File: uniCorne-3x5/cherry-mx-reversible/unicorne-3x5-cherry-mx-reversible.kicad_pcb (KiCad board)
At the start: 2 copper layers, 114.7 x 91.4 mm, 87 parts, among them J1 MJ-4PP-9, J2 Nice!View, J3 Conn_01x02, J4 Conn_01x03, SW1 SW_MX_HS, SW10 SW_MX_HS, SW11 SW_MX_HS, SW12 SW_MX_HS, SW13 SW_MX_HS, SW14 SW_MX_HS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

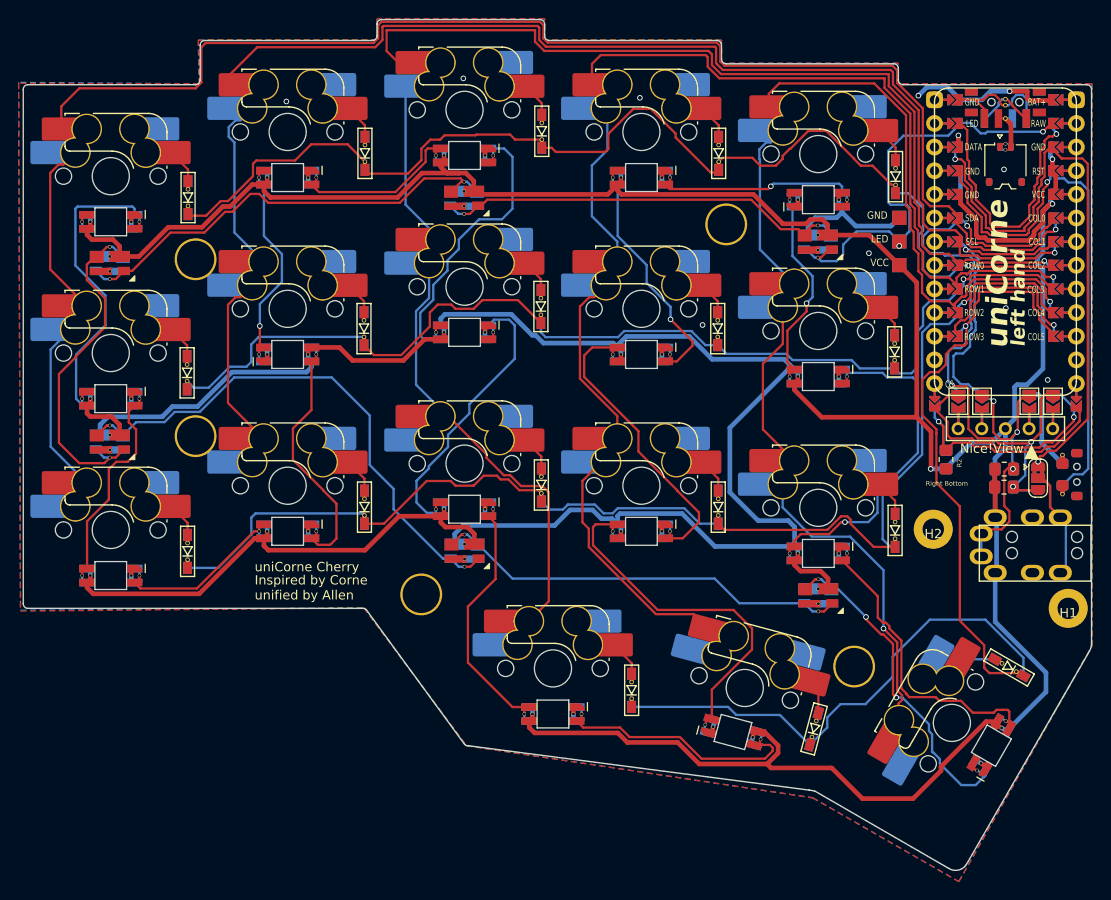
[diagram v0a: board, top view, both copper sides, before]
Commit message: amended cherry mx 3x5
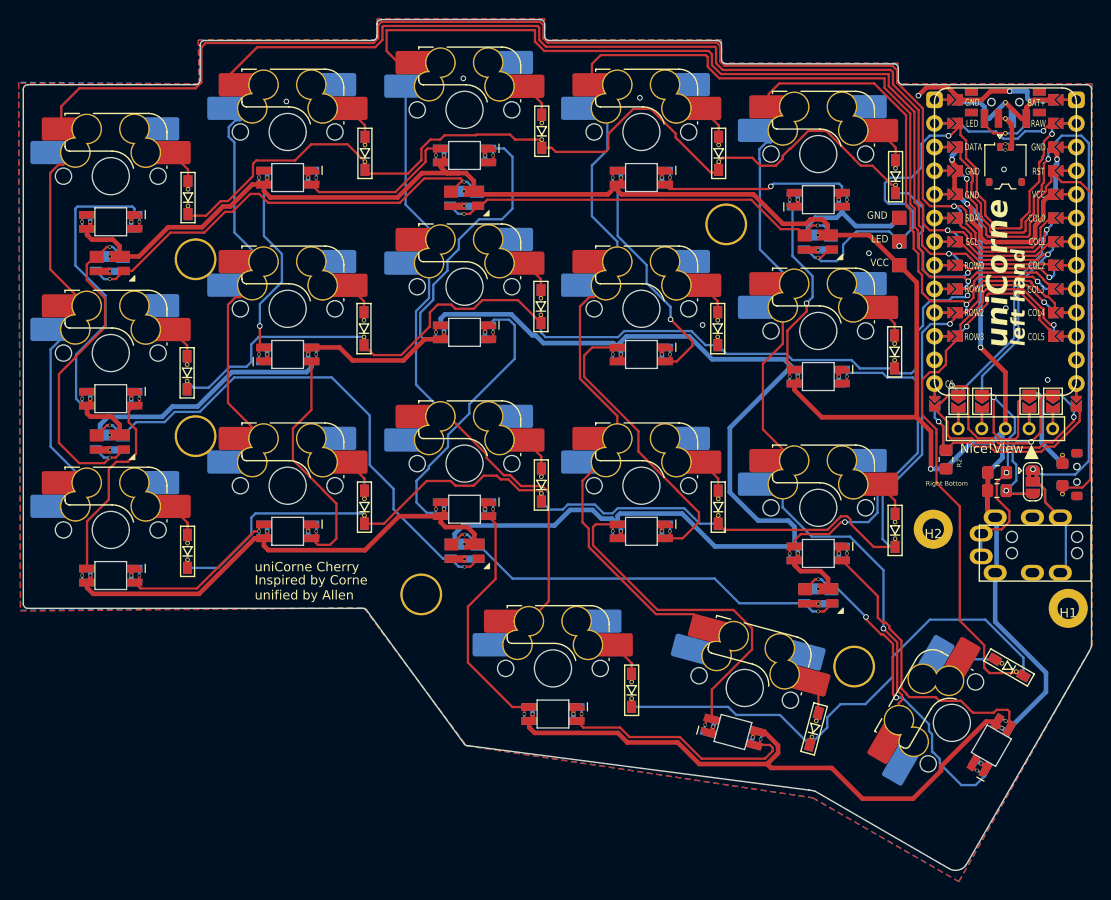
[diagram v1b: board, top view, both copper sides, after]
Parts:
- U1: footprint TB2086_MISC:ProMicro-ish-dn-rev-unrouted_3x5 -> TB2086_MISC:ProMicro-ish-dn-rev-unrouted_3x6
- moved R3 0.85 mm to (184.6, 109.8)
- moved R4 0.85 mm to (184.5, 111.7)
- moved JP9 0.70 mm to (188.4, 110.8)
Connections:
- PSW1 pad 1: unconnected-(PSW1-A-Pad1) -> BAT+
- PSW1 pad 3: BAT+ -> unconnected-(PSW1-C-Pad3)
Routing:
- net LED: track 46.5 -> 64.9 mm, vias 2 -> 3
- net unconnected-(U1-RAW-Pad24): track 28.3 -> 11.0 mm
- net unconnected-(PSW1-C-Pad3): track 0.00 -> 6.54 mm
- net unconnected-(PSW1-A-Pad1): track 6.23 -> 0.00 mm
- net DATA: track 64.8 -> 70.5 mm
- net SCL: track 60.3 -> 64.7 mm, vias 4 -> 3
- net GND: track 34.8 -> 38.3 mm
- net row0: track 123.0 -> 126.3 mm, vias 1 -> 2
- net BAT+: track 17.4 -> 14.2 mm
- net unconnected-(U1-B3-Pad15): track 18.6 -> 15.8 mm
- net row3: track 117.9 -> 115.6 mm
- net RESET: track 58.8 -> 60.3 mm
- net SDA: track 72.5 -> 71.1 mm
- net col2: track 166.6 -> 167.8 mm
- net col3: track 143.3 -> 142.4 mm
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
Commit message: amended chocolate 3x5
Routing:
- net SDA: track 71.1 -> 70.0 mm
- net row2: track 131.9 -> 131.2 mm
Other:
- board text added: "uniCorne Cherry 3x5"
- board text removed: "uniCorne Cherry"

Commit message: small tweak
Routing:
- net DATA: track 70.5 -> 76.6 mm
- net RESET: track 60.3 -> 62.9 mm
- net SDA: track 70.0 -> 68.6 mm
- net unconnected-(PSW1-C-Pad3): track 6.54 -> 5.31 mm
- net SCL: track 64.7 -> 63.6 mm
- net Net-(JP9-C): track 15.4 -> 14.5 mm
- net row0: track 126.3 -> 125.7 mm
- net col2: track 167.8 -> 167.2 mm

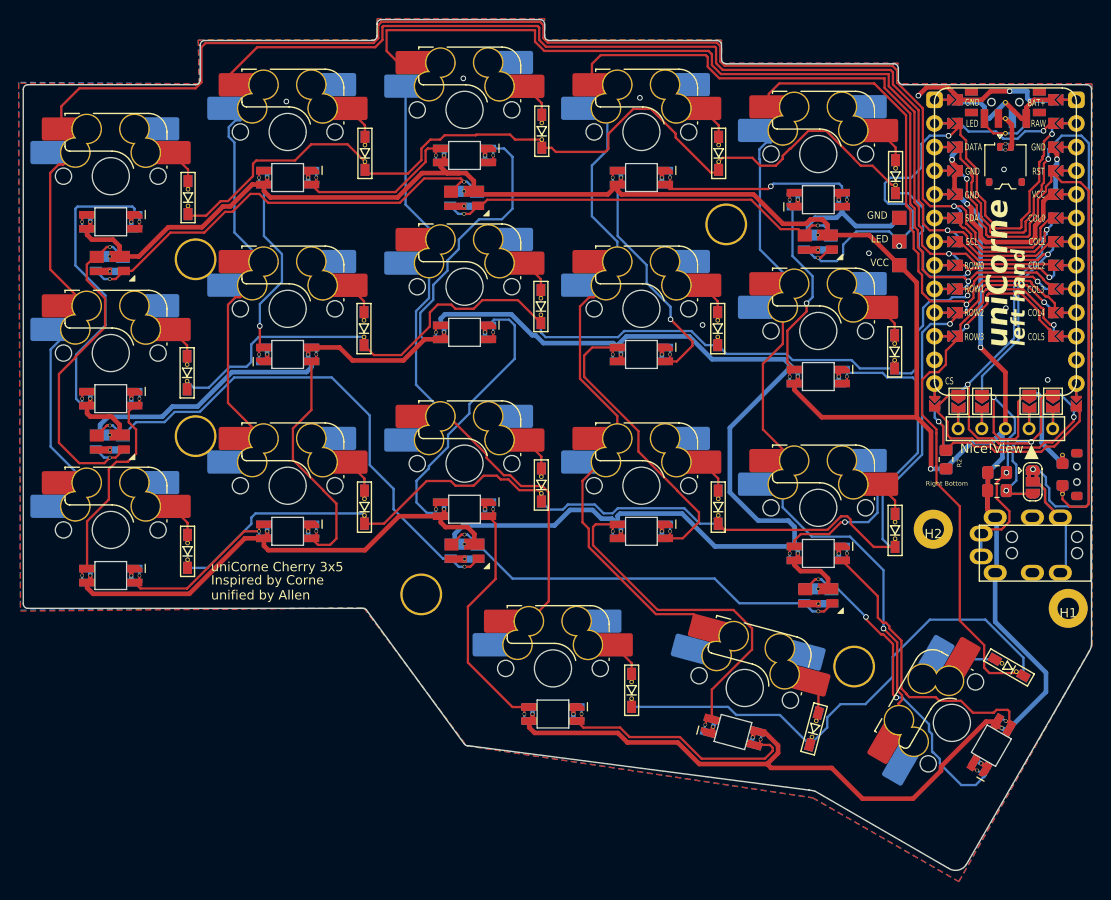
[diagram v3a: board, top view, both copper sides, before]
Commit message: amended footprint for LED
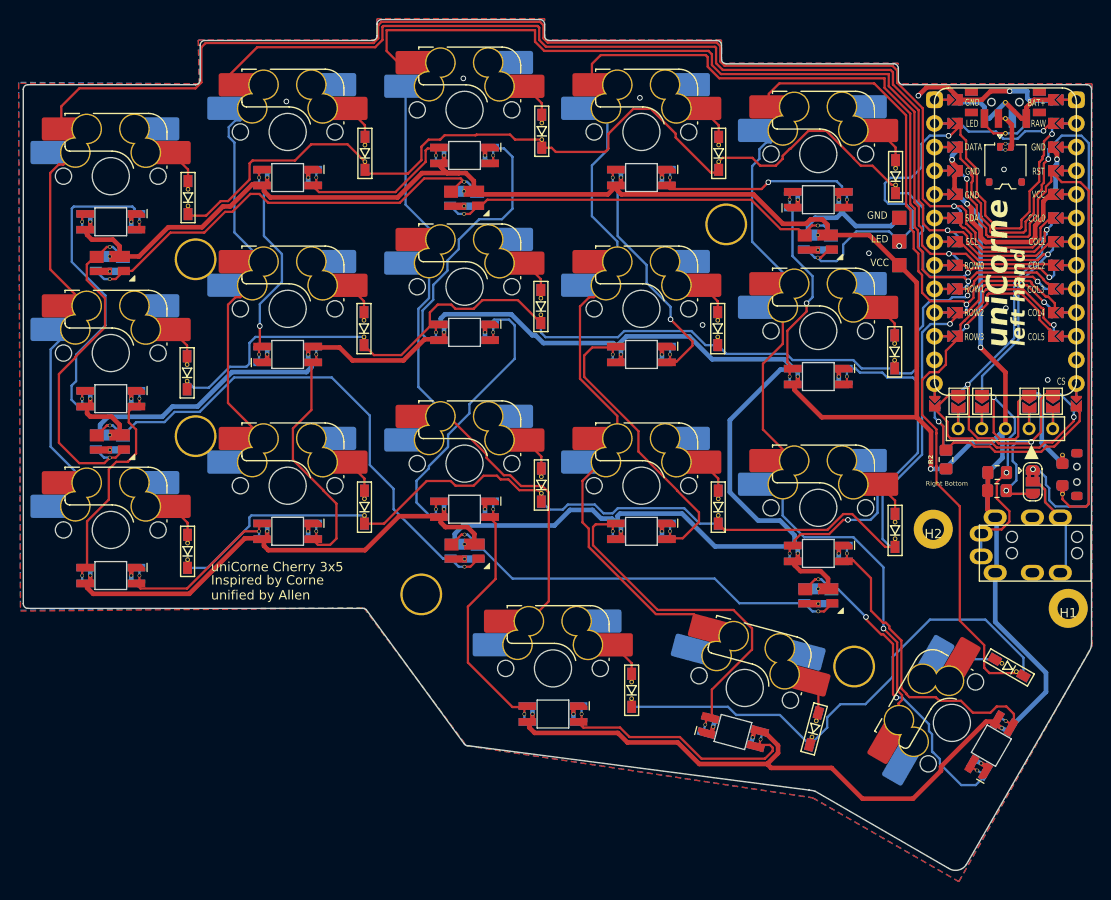
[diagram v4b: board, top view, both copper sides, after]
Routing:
- net Net-(L15-DIN): track 31.3 -> 32.9 mm
- net col4: track 131.7 -> 133.0 mm
- net Net-(L1-DIN): track 31.3 -> 32.6 mm
- net Net-(L13-DOUT): track 29.3 -> 29.9 mm

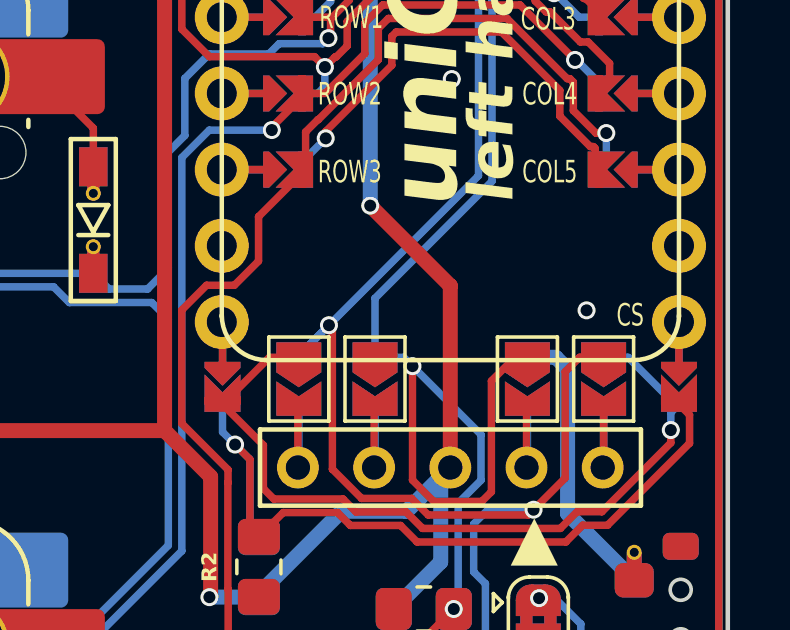
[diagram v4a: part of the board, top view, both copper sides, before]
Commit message: fixed footprint for promicro-ish 3x6
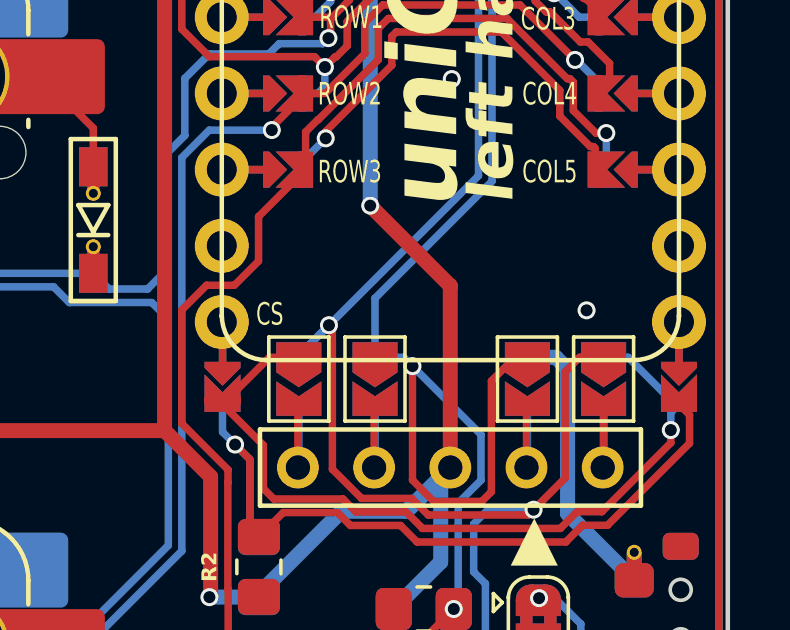
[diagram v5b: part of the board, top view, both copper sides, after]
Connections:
- U1 pad 12: IS_LEFT -> CS
- U1 pad 13: CS -> IS_LEFT

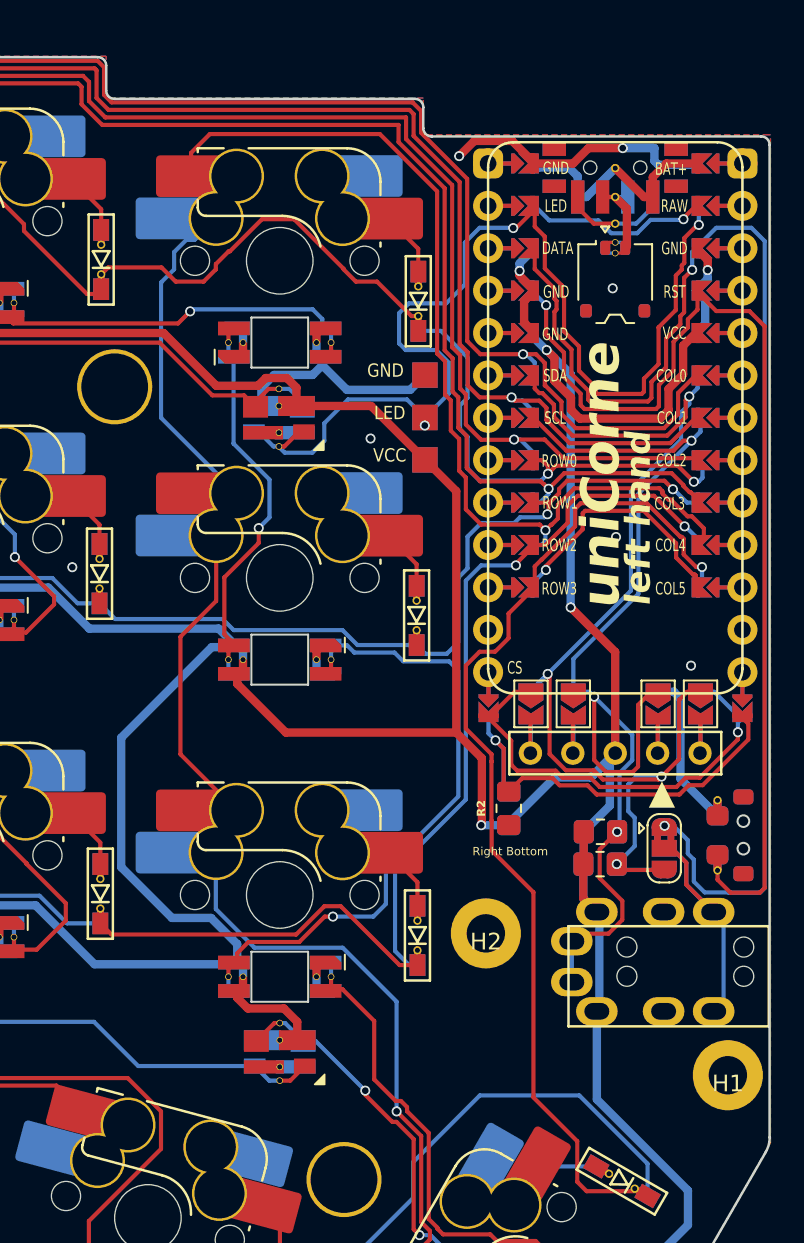
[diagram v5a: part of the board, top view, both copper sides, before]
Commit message: Bug fix scl (#3)
* fixed 3x5 hyprid mx

* fixed 3x5

* fixed 3x6
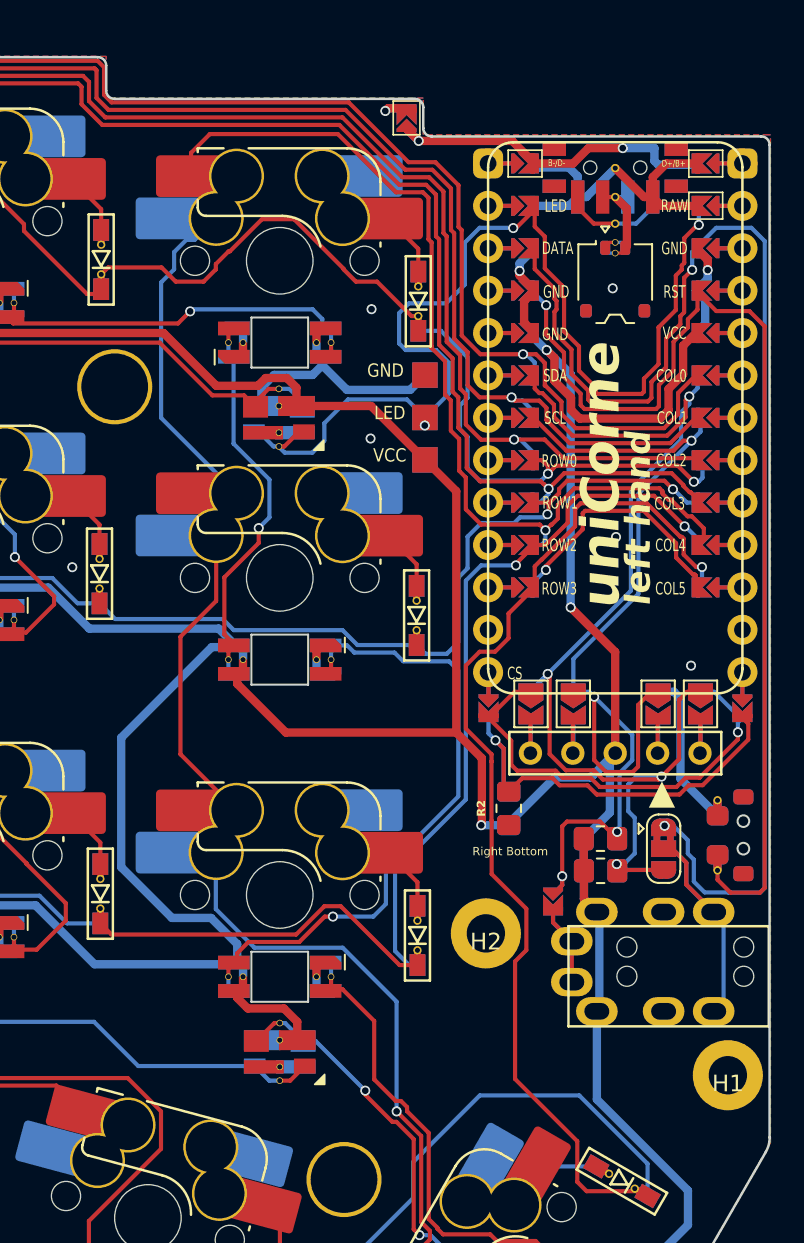
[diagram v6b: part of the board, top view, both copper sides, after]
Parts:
- added JP10: Jumper_3_Bridged12, TB2086_MISC:SolderJumper-3_P1.3mm_Bridged2Bar12_RoundedPad1.0x1.5mm_rev, F.Cu at (188.3, 110.8)
- added JP11: , TB2086_MISC:SolderJumper-2_P1.3mm_Open_TrianglePad1.0x1.2mm_rev, F.Cu at (172.9, 67.0)
- JP9: value Jumper_3_Bridged12 -> (none); footprint TB2086_MISC:SolderJumper-3_P1.3mm_Bridged2Bar12_RoundedPad1.0x1.5mm_rev -> TB2086_MISC:SolderJumper-2_P1.3mm_Open_TrianglePad1.0x1.2mm_rev
- U1: footprint TB2086_MISC:ProMicro-ish-dn-rev-unrouted_3x6 -> TB2086_MISC:ProMicro-ish-dn-rev-unrouted_3x5
- moved JP9 7.39 mm to (181.7, 113.9), turned to 90 degrees
- moved R3 0.41 mm to (184.6, 110.2)
- moved R4 0.40 mm to (184.6, 112.1)
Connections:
- J1 pad A: SCL -> Net-(JP9-B)
- J1 pad B: Net-(JP9-C) -> Net-(JP10-C)
- JP9 pad 1: DATA -> SCL
- JP9 pad 2: Net-(JP9-C) -> Net-(JP9-B)
- U1 pad 24: unconnected-(U1-RAW-Pad24) -> BAT+
- U1 pad 26: GND -> B-/D-
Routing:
- net B-/D-: track 0.00 -> 20.9 mm, vias 0 -> 2
- net Net-(JP9-C): track 14.5 -> 0.00 mm
- net Net-(JP10-C): track 0.00 -> 14.5 mm
- net GND: track 38.3 -> 24.6 mm
- net unconnected-(U1-RAW-Pad24): track 11.0 -> 0.00 mm, vias 1 -> 0
- net Net-(JP9-B): track 0.00 -> 6.97 mm
- net BAT+: track 14.2 -> 19.8 mm
- net SCL: track 63.6 -> 61.4 mm, vias 3 -> 4
- net col1: track 152.5 -> 151.2 mm
- net col0: track 177.2 -> 175.9 mm
- net col2: track 167.0 -> 165.8 mm
- net VCC: track 529.3 -> 528.0 mm
- net col3: track 142.1 -> 140.9 mm
- net row3: track 115.6 -> 116.2 mm
